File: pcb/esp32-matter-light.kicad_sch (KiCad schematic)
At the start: 14 parts, among them J1 IO, Q1 2N7000, SW1 SW_Push, U1 EKMC1607111, U2 Seeed Studio XIAO ESP32C6, U3 OSRB38C9AA

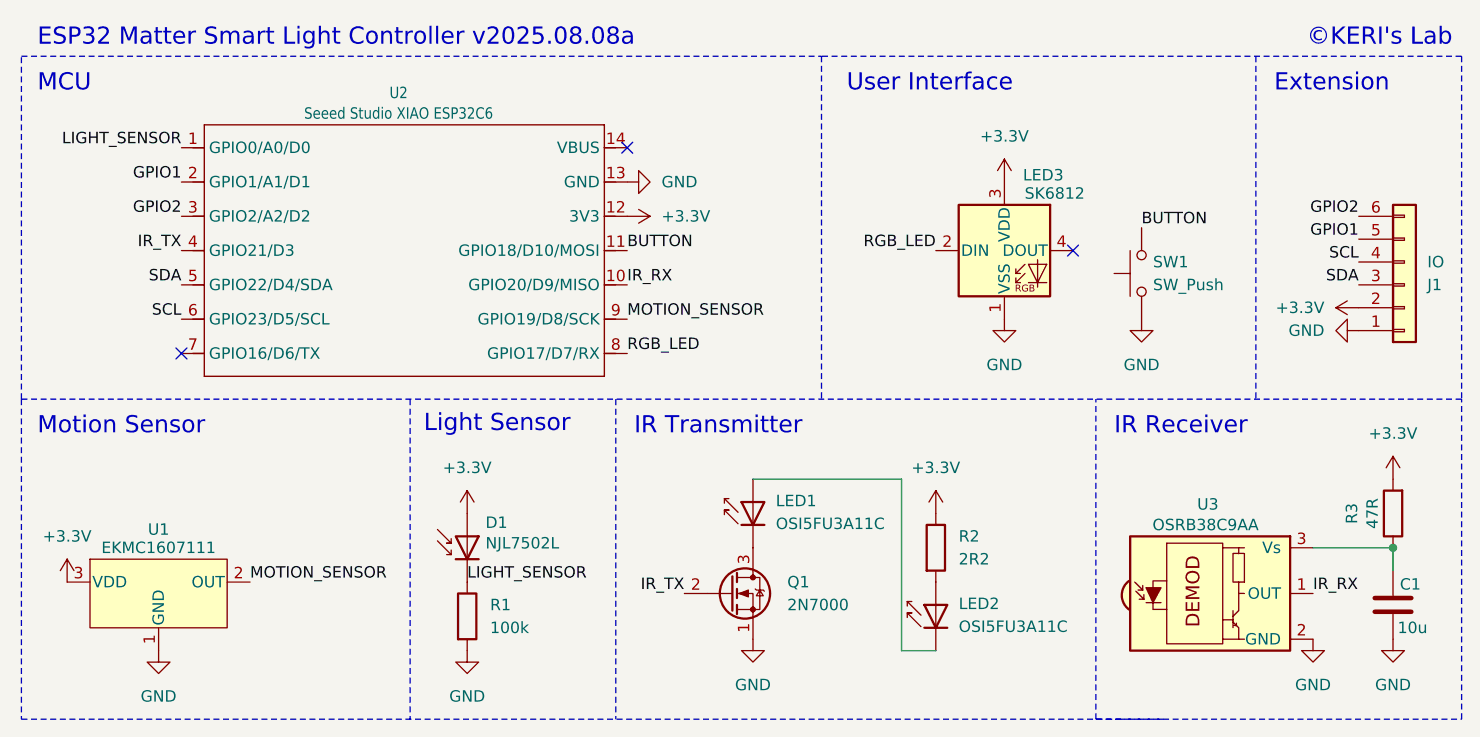
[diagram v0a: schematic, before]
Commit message: update pin assign
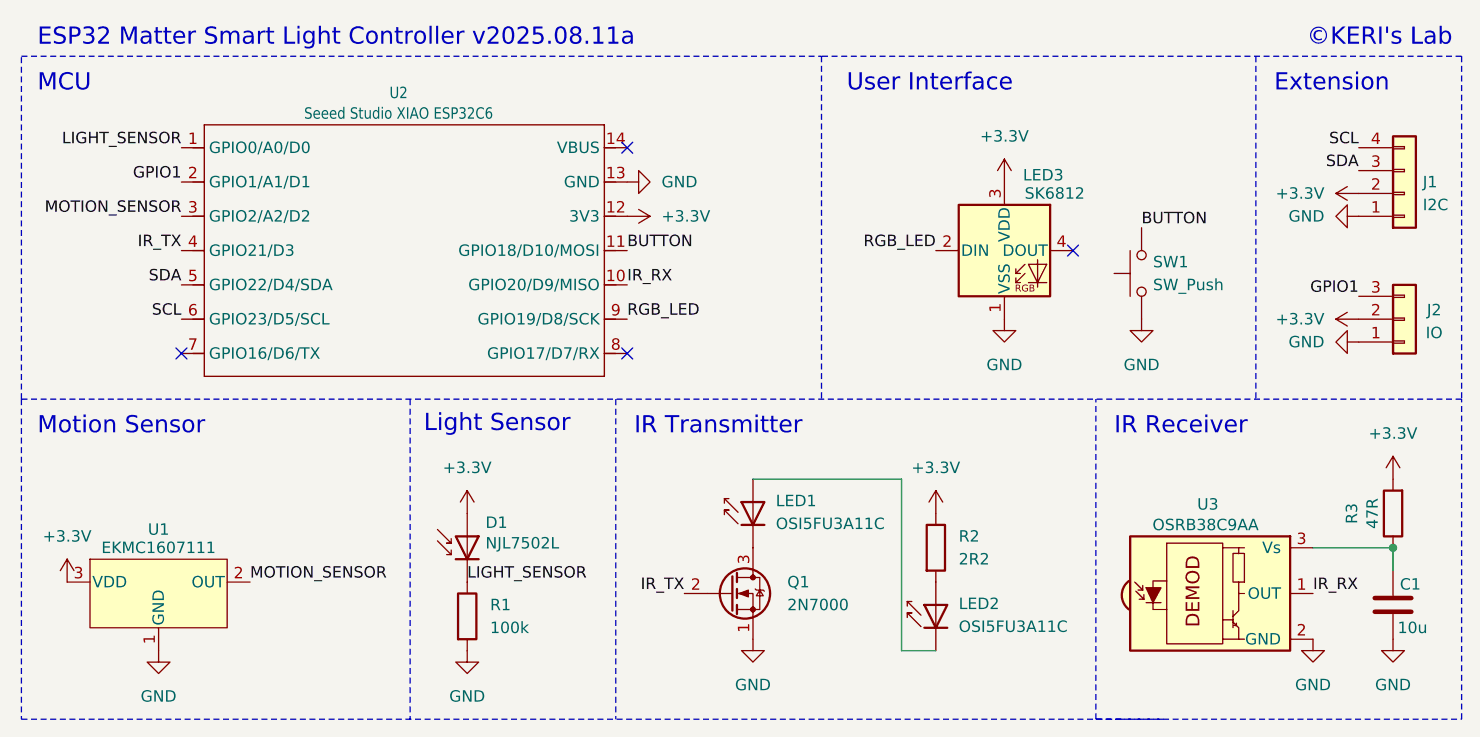
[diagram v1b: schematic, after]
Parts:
- added J2: IO, symbol Connector_Generic:Conn_01x03
- J1: value IO -> I2C; symbol Connector_Generic:Conn_01x06 -> Connector_Generic:Conn_01x04
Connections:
- net +3.3V: now also J2.2 (Pin_2)
- net GND: now also J2.1 (Pin_1)
- net GPIO1: now also J2.3 (Pin_3); no longer J1.5 (Pin_5)
- net MOTION_SENSOR: now also U2.3 (GPIO2/A2/D2); no longer U2.9 (GPIO19/D8/SCK)
- net RGB_LED: now also U2.9 (GPIO19/D8/SCK); no longer U2.8 (GPIO17/D7/RX)
- removed net GPIO2: J1.6 (Pin_6), U2.3 (GPIO2/A2/D2)
- no-connect marks 3 -> 4
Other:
- note added: "ESP32 Matter Smart Light Controller v2025.08.11a"
- note removed: "ESP32 Matter Smart Light Controller v2025.08.08a"
